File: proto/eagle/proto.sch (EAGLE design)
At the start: 38 parts, among them U1 ARDUINO_MINI_PRO, U2 ATA6663, U3 7805T, U4 FTDI-BOARD

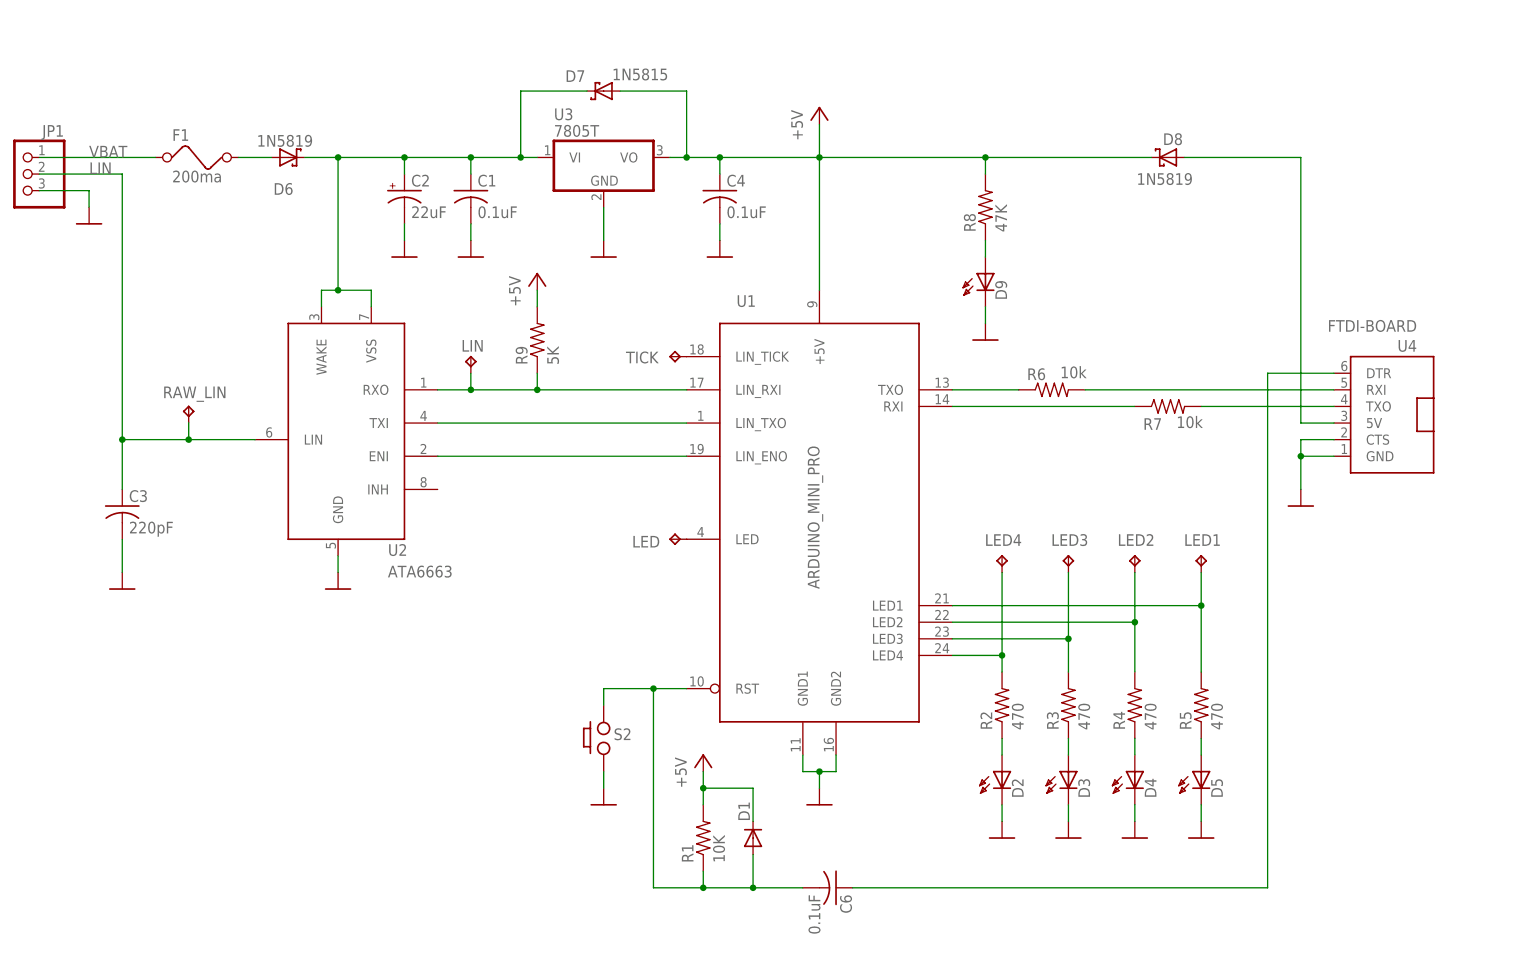
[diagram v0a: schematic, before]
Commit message: Updated the schema.
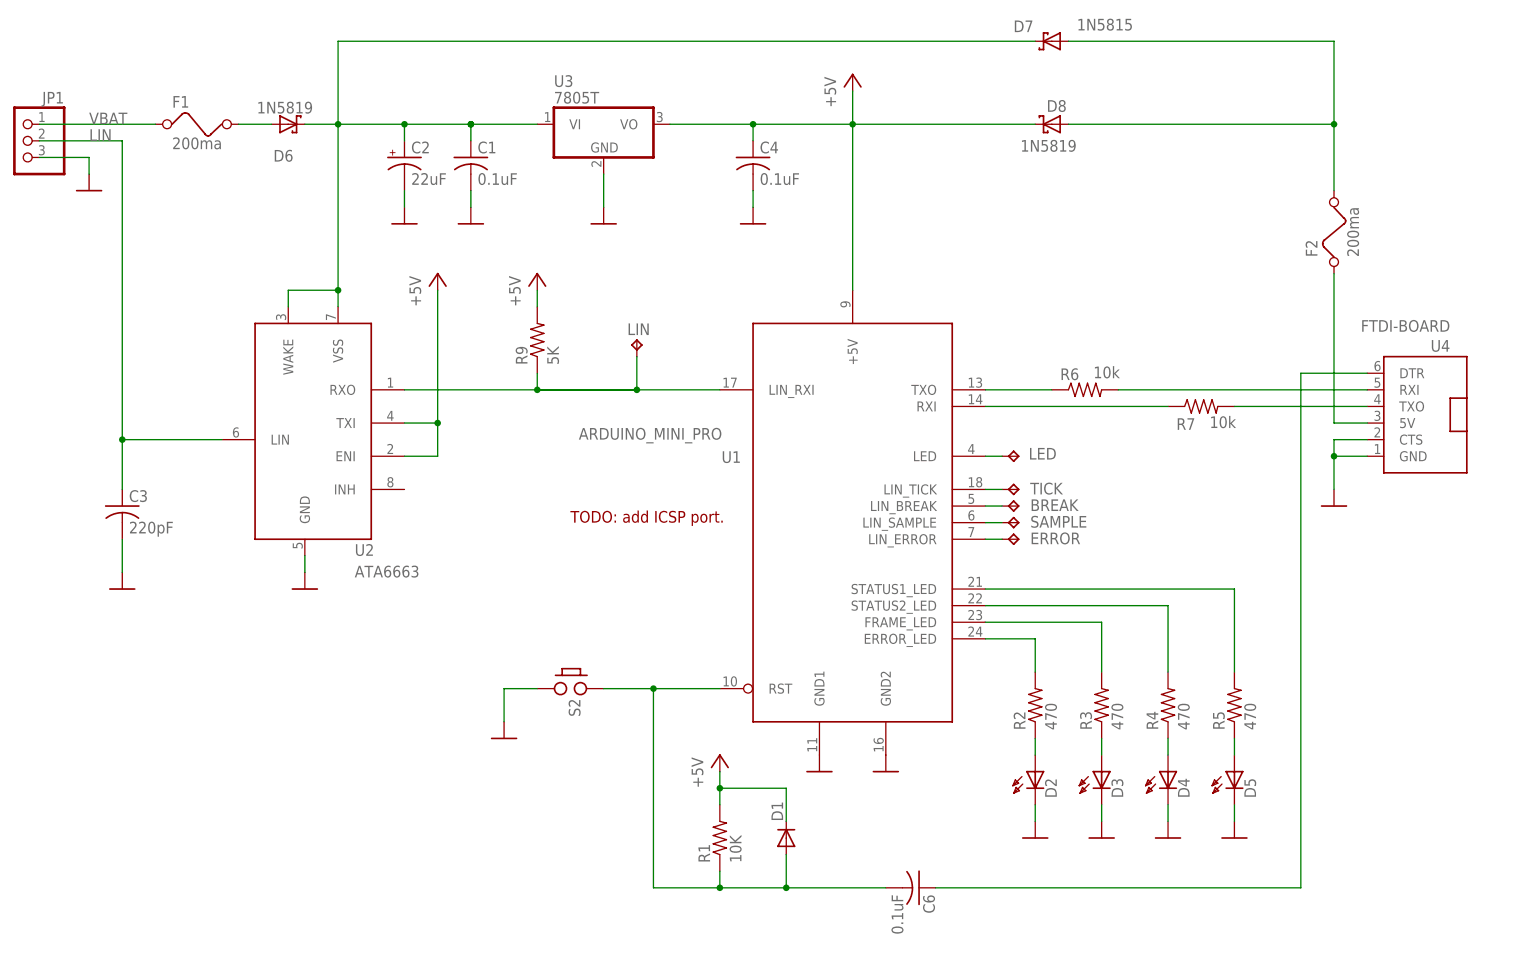
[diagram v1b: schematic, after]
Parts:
- removed D9: HLMP6, display-hp:HLMP6
- removed LED1, LED2, LED3, LED4, RAW_LIN: TPPAD1-17, testpad:TPPAD1-17
- removed R8: 47K, rcl:R-US_R0805
- added BREAK, ERROR, SAMPLE: TPPAD1-17, testpad:TPPAD1-17
- added F2: 200ma, special:FUSE
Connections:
- removed net N$17: D8.A, U4.5V
- removed net N$19: U1.LIN_TXO, U2.TXI
- removed net N$20: U1.LIN_ENO, U2.ENI
- removed net N$25: D9.A, R8.1
- new net N$11: ERROR.TP, U1.LIN_ERROR
- new net N$12: D7.A, D8.A, F2.2
- new net N$16: F2.1, U4.5V
- new net N$5: BREAK.TP, U1.LIN_BREAK
- new net N$6: SAMPLE.TP, U1.LIN_SAMPLE
- net +5V: now also U2.ENI, U2.TXI; no longer D7.A, R8.2
- net GND: now also S2.P$4; no longer D9.K
- net LIN: no longer RAW_LIN.TP
- net N$10: now also U1.STATUS1_LED; no longer LED1.TP, U1.LED1
- net N$7: now also U1.ERROR_LED; no longer LED4.TP, U1.LED4
- net N$8: now also U1.FRAME_LED; no longer LED3.TP, U1.LED3
- net N$9: now also U1.STATUS2_LED; no longer LED2.TP, U1.LED2
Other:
- note added: "TODO: add ICSP port."
- moved on the sheet: C1, C2, C4, C6, D1, D2, D3, D4, D5, D6, D7, D8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

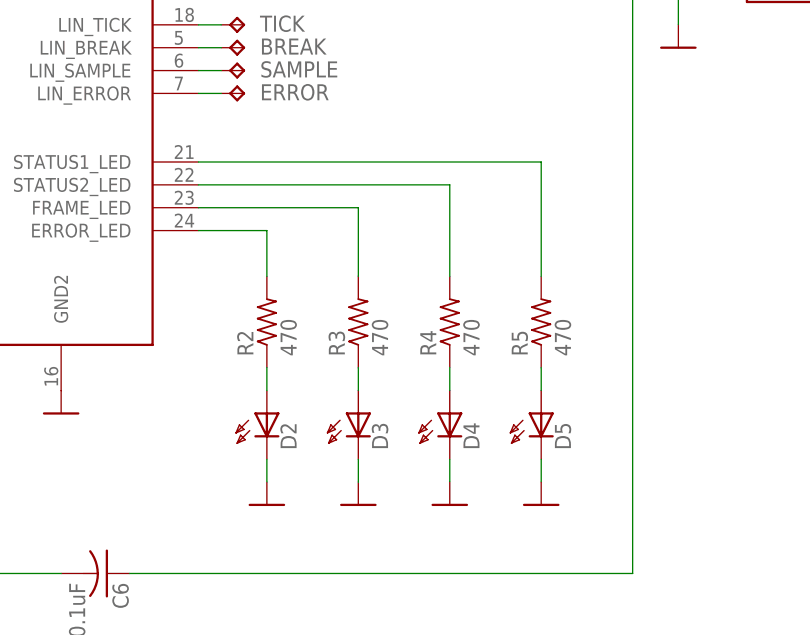
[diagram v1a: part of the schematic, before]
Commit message: Updated schema: increased resistor of red LED. Added LED color values.
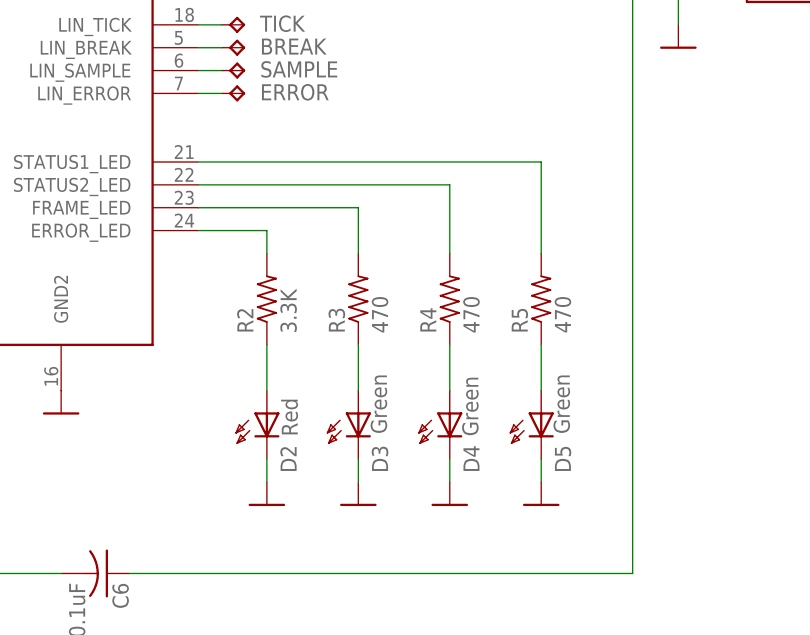
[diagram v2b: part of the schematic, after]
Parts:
- D2: value HLMP6 -> Red
- D3, D4, D5: value HLMP6 -> Green
- R2: value 470 -> 3.3K
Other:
- moved on the sheet: R2, R3, R4, R5
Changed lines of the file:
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@@
 </classes>
 <parts>
-<part name="R2" library="rcl" deviceset="R-US_" device="R0805" value="470"/>
+<part name="R2" library="rcl" deviceset="R-US_" device="R0805" value="3.3K"/>
 <part name="R3" library="rcl" deviceset="R-US_" device="R0805" value="470"/>
 <part name="R4" library="rcl" deviceset="R-US_" device="R0805" value="470"/>
 <part name="R5" library="rcl" deviceset="R-US_" device="R0805" value="470"/>
-<part name="D2" library="display-hp" deviceset="HLMP6" device="" value=""/>
-<part name="D3" library="display-hp" deviceset="HLMP6" device="" value=""/>
-<part name="D4" library="display-hp" deviceset="HLMP6" device="" value=""/>
-<part name="D5" library="display-hp" deviceset="HLMP6" device="" value=""/>
+<part name="D2" library="display-hp" deviceset="HLMP6" device="" value="Red"/>
+<part name="D3" library="display-hp" deviceset="HLMP6" device="" value="Green"/>
+<part name="D4" library="display-hp" deviceset="HLMP6" device="" value="Green"/>
+<part name="D5" library="display-hp" deviceset="HLMP6" device="" value="Green"/>
 <part name="S2" library="my_lib" deviceset="PUSH_BUTTON" device=""/>
 <part name="U2" library="my_lib" deviceset="ATA6663" device=""/>
@@
 </plain>
 <instances>
-<instance part="R2" gate="G$1" x="228.6" y="99.06" rot="R90"/>
-<instance part="R3" gate="G$1" x="238.76" y="99.06" rot="R90"/>
-<instance part="R4" gate="G$1" x="248.92" y="99.06" rot="R90"/>
-<instance part="R5" gate="G$1" x="259.08" y="99.06" rot="R90"/>
-<instance part="D2" gate="A" x="228.6" y="86.36"/>
-<instance part="D3" gate="A" x="238.76" y="86.36"/>
-<instance part="D4" gate="A" x="248.92" y="86.36"/>
-<instance part="D5" gate="A" x="259.08" y="86.36"/>
+<instance part="R2" gate="G$1" x="228.6" y="101.6" rot="R90"/>
+<instance part="R3" gate="G$1" x="238.76" y="101.6" rot="R90"/>
+<instance part="R4" gate="G$1" x="248.92" y="101.6" rot="R90"/>
+<instance part="R5" gate="G$1" x="259.08" y="101.6" rot="R90"/>
+<instance part="D2" gate="A" x="228.6" y="86.36" smashed="yes">
+<attribute name="NAME" x="231.902" y="82.296" size="1.778" layer="95" rot="R90"/>
+<attribute name="VALUE" x="232.029" y="86.36" size="1.778" layer="96" rot="R90"/>
+</instance>
+<instance part="D3" gate="A" x="238.76" y="86.36" smashed="yes">
+<attribute name="NAME" x="242.062" y="82.296" size="1.778" layer="95" rot="R90"/>
+<attribute name="VALUE" x="241.935" y="86.614" size="1.778" layer="96" rot="R90"/>
+</instance>
+<instance part="D4" gate="A" x="248.92" y="86.36" smashed="yes">
+<attribute name="NAME" x="252.222" y="82.296" size="1.778" layer="95" rot="R90"/>
+<attribute name="VALUE" x="252.095" y="86.36" size="1.778" layer="96" rot="R90"/>
+</instance>
+<instance part="D5" gate="A" x="259.08" y="86.36" smashed="yes">
+<attribute name="NAME" x="262.382" y="82.296" size="1.778" layer="95" rot="R90"/>
+<attribute name="VALUE" x="262.255" y="86.614" size="1.778" layer="96" rot="R90"/>
+</instance>
 <instance part="S2" gate="G$1" x="157.48" y="101.6" rot="R270"/>
 <instance part="U2" gate="G$1" x="116.84" y="142.24" smashed="yes">
@@
 <pinref part="R5" gate="G$1" pin="1"/>
 <pinref part="D5" gate="A" pin="A"/>
-<wire x1="259.08" y1="93.98" x2="259.08" y2="91.44" width="0.1524" layer="91"/>
+<wire x1="259.08" y1="96.52" x2="259.08" y2="91.44" width="0.1524" layer="91"/>
 </segment>
 </net>
@@
 <pinref part="R4" gate="G$1" pin="1"/>
 <pinref part="D4" gate="A" pin="A"/>
-<wire x1="248.92" y1="93.98" x2="248.92" y2="91.44" width="0.1524" layer="91"/>
+<wire x1="248.92" y1="96.52" x2="248.92" y2="91.44" width="0.1524" layer="91"/>
 </segment>
 </net>
@@
 <pinref part="R3" gate="G$1" pin="1"/>
 <pinref part="D3" gate="A" pin="A"/>
-<wire x1="238.76" y1="93.98" x2="238.76" y2="91.44" width="0.1524" layer="91"/>
+<wire x1="238.76" y1="96.52" x2="238.76" y2="91.44" width="0.1524" layer="91"/>
 </segment>
 </net>
@@
 <pinref part="R2" gate="G$1" pin="1"/>
 <pinref part="D2" gate="A" pin="A"/>
-<wire x1="228.6" y1="93.98" x2="228.6" y2="91.44" width="0.1524" layer="91"/>
+<wire x1="228.6" y1="96.52" x2="228.6" y2="91.44" width="0.1524" layer="91"/>
 </segment>
 </net>
@@
 <pinref part="U1" gate="G$1" pin="ERROR_LED"/>
 <wire x1="220.98" y1="109.22" x2="228.6" y2="109.22" width="0.1524" layer="91"/>
-<wire x1="228.6" y1="109.22" x2="228.6" y2="104.14" width="0.1524" layer="91"/>
+<wire x1="228.6" y1="109.22" x2="228.6" y2="106.68" width="0.1524" layer="91"/>
 </segment>
 </net>
@@
 <segment>
 <pinref part="R3" gate="G$1" pin="2"/>
-<wire x1="238.76" y1="111.76" x2="238.76" y2="104.14" width="0.1524" layer="91"/>
+<wire x1="238.76" y1="111.76" x2="238.76" y2="106.68" width="0.1524" layer="91"/>
 <pinref part="U1" gate="G$1" pin="FRAME_LED"/>
 <wire x1="220.98" y1="111.76" x2="238.76" y2="111.76" width="0.1524" layer="91"/>
@@
 <segment>
 <pinref part="R4" gate="G$1" pin="2"/>
-<wire x1="248.92" y1="114.3" x2="248.92" y2="104.14" width="0.1524" layer="91"/>
+<wire x1="248.92" y1="114.3" x2="248.92" y2="106.68" width="0.1524" layer="91"/>
 <pinref part="U1" gate="G$1" pin="STATUS2_LED"/>
 <wire x1="220.98" y1="114.3" x2="248.92" y2="114.3" width="0.1524" layer="91"/>
@@
 <segment>
 <pinref part="R5" gate="G$1" pin="2"/>
-<wire x1="259.08" y1="116.84" x2="259.08" y2="104.14" width="0.1524" layer="91"/>
+<wire x1="259.08" y1="116.84" x2="259.08" y2="106.68" width="0.1524" layer="91"/>
 <pinref part="U1" gate="G$1" pin="STATUS1_LED"/>
 <wire x1="220.98" y1="116.84" x2="259.08" y2="116.84" width="0.1524" layer="91"/>

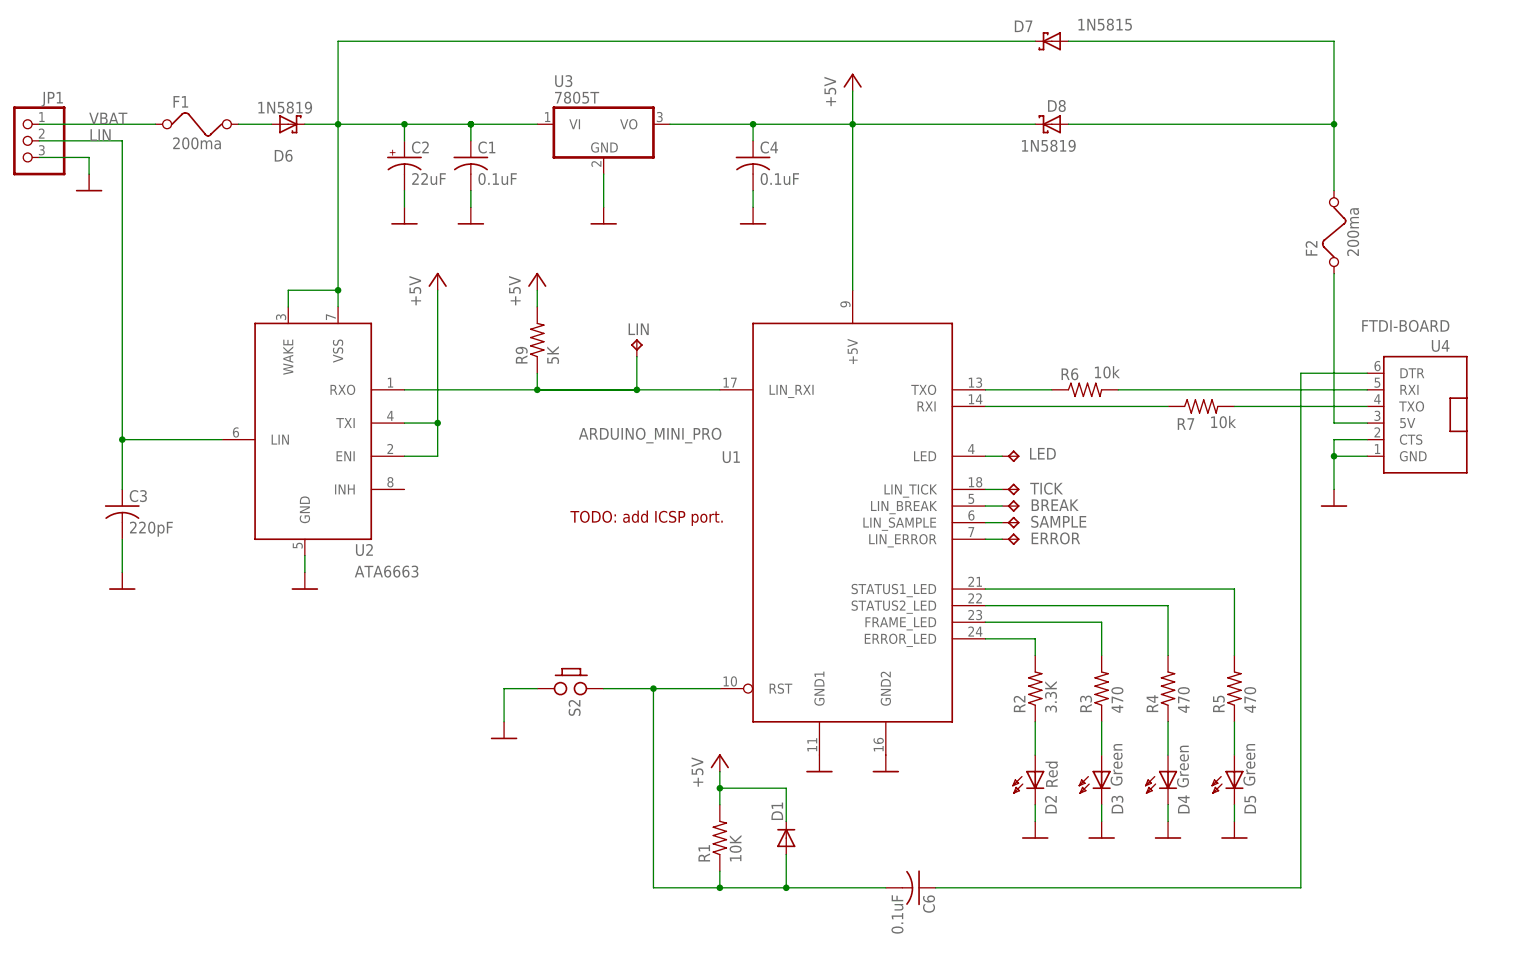
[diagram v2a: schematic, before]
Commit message: Added an ICSP port to the schema.
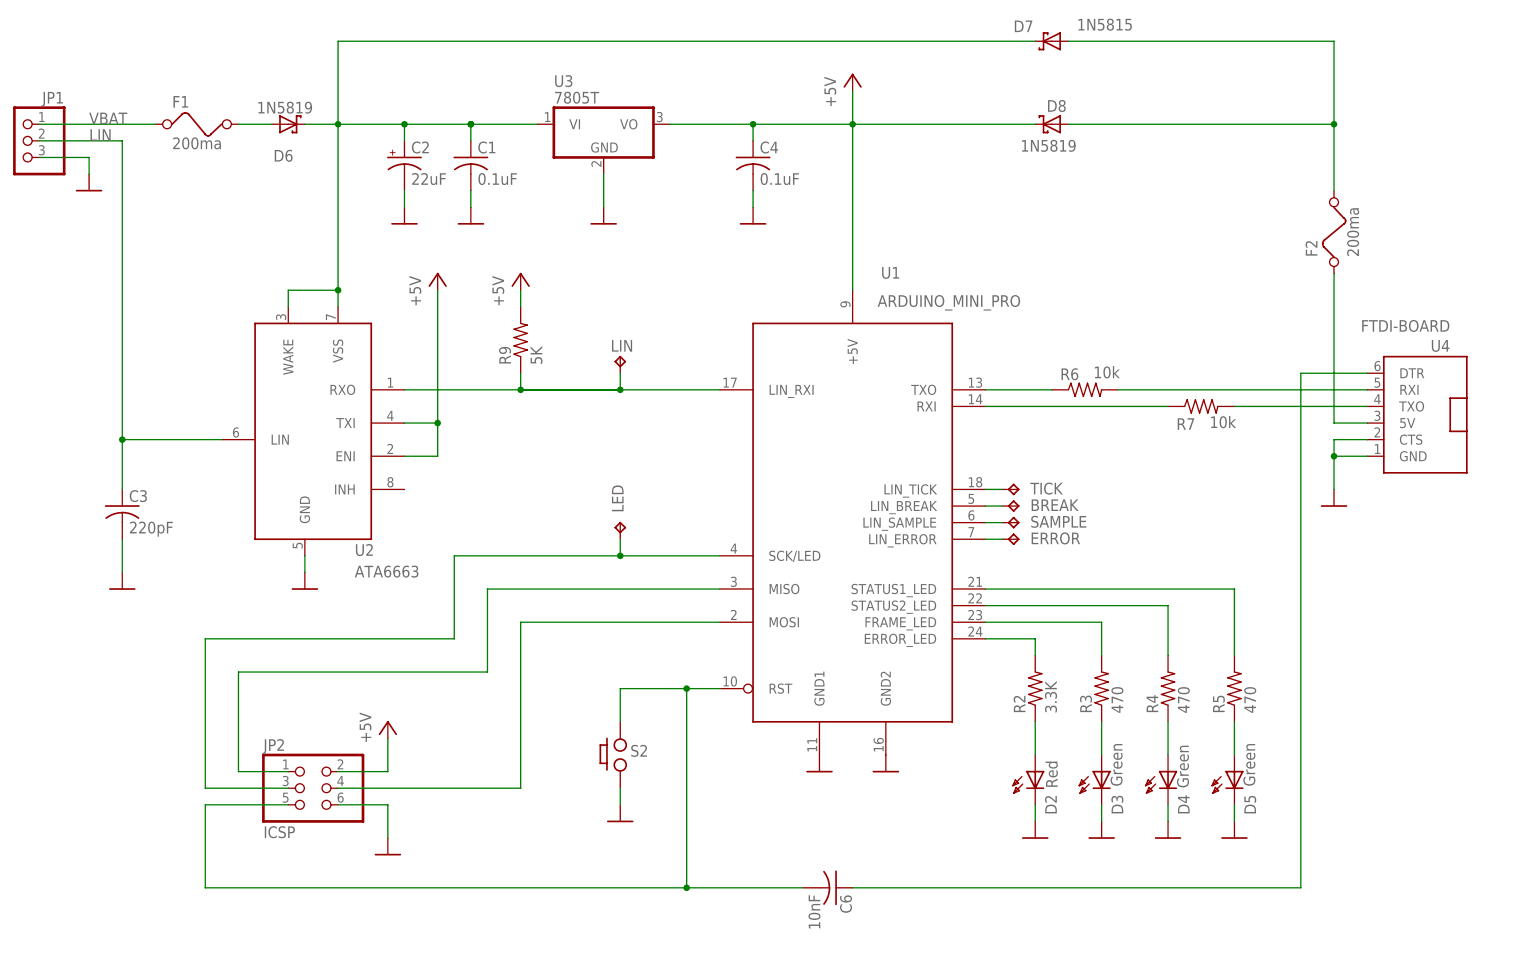
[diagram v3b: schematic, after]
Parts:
- removed D1: (no value), diode:DIODE-DO214BA
- removed R1: 10K, rcl:R-US_R0805
- added JP2: ICSP, pinhead:PINHD-2X3
- C6: value 0.1uF -> 10nF
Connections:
- removed net N$27: LED.TP, U1.LED
- new net N$20: JP2.4, U1.MOSI
- new net N$25: JP2.1, U1.MISO
- new net N$28: JP2.3, LED.TP, U1.SCK/LED
- net +5V: now also JP2.2; no longer D1.C, R1.2
- net GND: now also JP2.6
- net N$15: now also JP2.5; no longer D1.A, R1.1
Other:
- note removed: "TODO: add ICSP port."
- moved on the sheet: C6, LED, LIN, R9, S2
